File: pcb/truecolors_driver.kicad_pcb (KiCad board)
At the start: 4 copper layers, 70 x 90 mm, 66 parts, among them Q1 AOD413A(UMW), Q2 AOD413A(UMW), Q3 AOD413A(UMW), SW1 TS-1088-AR02016, U2 CH224A, U3 ESP32-S3-WROOM-1(N8R8), U4 AMS1117-3.3, U5 LM3409MY/NOPB, U6 LM3409MY/NOPB, U7 LM3409MY/NOPB

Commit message: update pcb
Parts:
- added C34: 10uF 25V, Capacitor_SMD:C_0603_1608Metric, F.Cu at (192.3, 124.2)
- added C35: 100nF 16V, Capacitor_SMD:C_0603_1608Metric, F.Cu at (191.1, 129.1)
- added C36: 10uF 25V, Capacitor_SMD:C_0603_1608Metric, F.Cu at (189.3, 119.7)
- added C37: 10uF 25V, Capacitor_SMD:C_0603_1608Metric, F.Cu at (189.3, 121.2)
- added C38: 10uF 25V, Capacitor_SMD:C_0603_1608Metric, F.Cu at (189.3, 122.7)
- added C39: 10uF 25V, Capacitor_SMD:C_0603_1608Metric, F.Cu at (189.3, 124.2)
- added C40: 100nF 16V, Capacitor_SMD:C_0603_1608Metric, F.Cu at (150.8, 134.5)
- added CN1: 1.0-3PWT, EasyEDA:CONN-SMD_3P-P1.00_C3029342, F.Cu at (140.7, 104.0)
- added CN2: 47053-1000, EasyEDA:CONN-TH_47053-1000, F.Cu at (143.8, 139.0)
- added L4: 4.7uH, EasyEDA:IND-SMD_L4.4-W4.2, F.Cu at (186.7, 127.5)
- added Q4: BSS138, Package_TO_SOT_SMD:SOT-23, F.Cu at (151.1, 140.0)
- added R17: 10k, Resistor_SMD:R_0603_1608Metric, F.Cu at (157.8, 85.1)
- added R18: 10k, Resistor_SMD:R_0603_1608Metric, F.Cu at (180.2, 85.1)
- added R19: 10k, Resistor_SMD:R_0603_1608Metric, F.Cu at (202.5, 85.1)
- added R20: 10k, Resistor_SMD:R_0603_1608Metric, F.Cu at (150.8, 133.1)
- added R21: 68k, Resistor_SMD:R_0603_1608Metric, F.Cu at (150.8, 136.0)
- added R22: 2k2, Resistor_SMD:R_0603_1608Metric, F.Cu at (168.2, 125.0)
- added R23: 2k2, Resistor_SMD:R_0603_1608Metric, F.Cu at (166.7, 125.0)
- added R24: 120k, Resistor_SMD:R_0603_1608Metric, F.Cu at (200.2, 126.5)
- added R25: 10k, Resistor_SMD:R_0603_1608Metric, F.Cu at (147.7, 134.0)
- added R26: 120k, Resistor_SMD:R_0603_1608Metric, F.Cu at (154.5, 138.3)
- added U1: AP63205WU-7, EasyEDA:TSOT-23-6_L2.9-W1.6-P0.95-LS2.8-BL, F.Cu at (191.8, 126.7)
- C1: value 1uF -> 1uF 50V; footprint Capacitor_SMD:C_0603_1608Metric_Pad1.08x0.95mm_HandSolder -> Capacitor_SMD:C_0603_1608Metric
- C10, C11, C12, C13, C14, C15, C16, C19, C20, C21, C22, C23, C24, C25, C26, C29, C30, C31, C32, C33, C4, C5, C6, C9: value 4.7uF -> 4.7uF 35V
- C17, C27, C7: value 1uF -> 1uF 50V
- C18, C28, C8: value 470pF -> 470pF 50V
- C2, C3: value 10uF -> 10uF 25V; footprint Capacitor_SMD:C_0603_1608Metric_Pad1.08x0.95mm_HandSolder -> Capacitor_SMD:C_0603_1608Metric
- moved C2 25.9 mm to (176.3, 137.8), turned to -90 degrees
- moved U4 21.2 mm to (170.6, 138.8), turned to 0 degrees
- moved C3 20.3 mm to (164.9, 140.1), turned to 180 degrees
- moved C1 2.59 mm to (205.7, 116.7), turned to 90 degrees
- moved C18 1.53 mm to (178.2, 82.8), turned to 180 degrees
- moved C28 1.53 mm to (200.6, 82.8), turned to 180 degrees
- moved C8 1.53 mm to (155.8, 82.8), turned to 180 degrees
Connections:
- U2 pad 10: /PD_PG -> unconnected-(U2-PG-Pad10)
- U2 pad 2: unconnected-(U2-CFG2/SCL-Pad2) -> /CH224A_SCL
- U2 pad 3: unconnected-(U2-CFG3/SDA-Pad3) -> /CH224A_SDA
- U2 pad 9: GND -> Net-(U2-CFG1)
- U3 pad 12: unconnected-(U3-IO8-Pad12) -> /CH224A_SDA
- U3 pad 17: unconnected-(U3-IO9-Pad17) -> /CH224A_SCL
- U3 pad 31: unconnected-(U3-IO38-Pad31) -> /EN_B
- U3 pad 32: unconnected-(U3-IO39-Pad32) -> /EN_G
- U3 pad 33: unconnected-(U3-IO40-Pad33) -> /EN_R
- U3 pad 4: unconnected-(U3-IO4-Pad4) -> /VIN_ADC
- U3 pad 6: unconnected-(U3-IO6-Pad6) -> /FAN_PWM
- U3 pad 7: unconnected-(U3-IO7-Pad7) -> /FAN_TACH
- U5 pad 3: /driverR/PWM -> /EN_R
- U6 pad 3: /driverG/PWM -> /EN_G
- U7 pad 3: /driverB/PWM -> /EN_B
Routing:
- net /EN_B: track 0.00 -> 70.9 mm
- net /CH224A_SDA: track 0.00 -> 57.8 mm, vias 0 -> 3
- net /CH224A_SCL: track 0.00 -> 53.9 mm, vias 0 -> 2
- net +20V: track 83.5 -> 135.7 mm, vias 21 -> 24
- net /EN_G: track 0.00 -> 49.9 mm
- net +5V: track 2.90 -> 50.8 mm, vias 0 -> 7
- net /EN_R: track 0.00 -> 31.6 mm
- net /FAN_TACH: track 0.00 -> 18.5 mm, vias 0 -> 1
- net /FAN_PWM: track 0.00 -> 13.4 mm
- net /RX: track 0.00 -> 13.2 mm
- net /TX: track 0.00 -> 11.0 mm
- net GND: track 2.77 -> 11.9 mm, vias 15 -> 29
- net Net-(U2-CFG1): track 0.00 -> 5.75 mm
- net Net-(U1-SW): track 0.00 -> 4.50 mm
- net /VIN_ADC: track 0.00 -> 4.48 mm
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- added copper zone on In2.Cu, net +5V

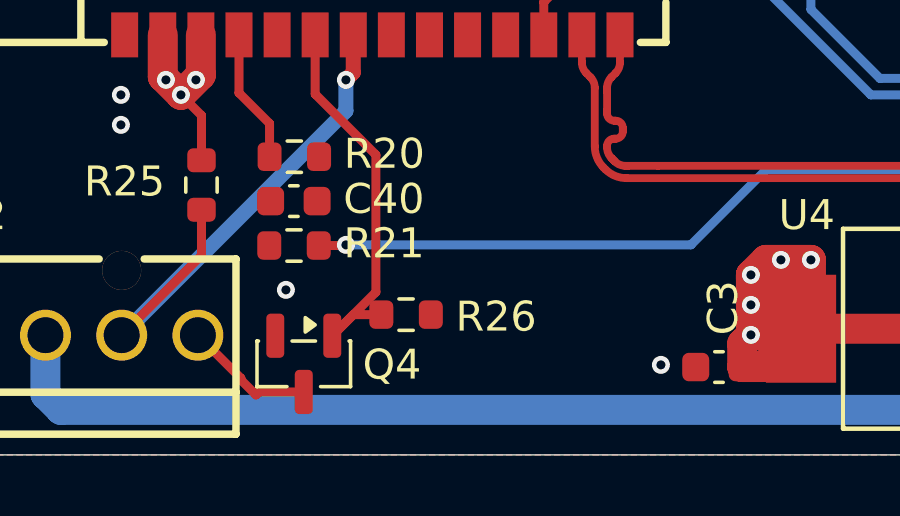
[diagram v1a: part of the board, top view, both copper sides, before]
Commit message: R26 pullup instead of pulldown for fan-off boot
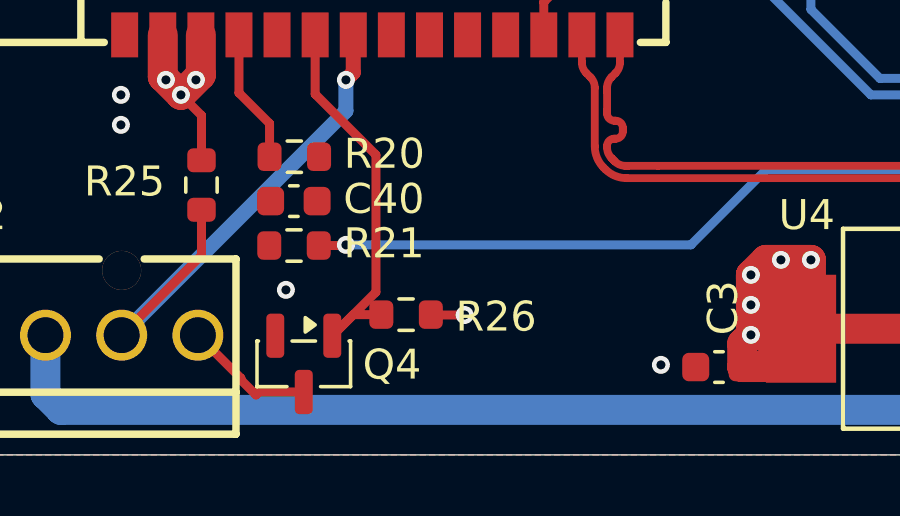
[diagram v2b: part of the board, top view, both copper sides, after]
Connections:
- R26 pad 2: GND -> +3.3V
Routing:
- net +3.3V: track 36.5 -> 37.6 mm, vias 10 -> 11
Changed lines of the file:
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@@
 			(layers "F.Cu" "F.Mask" "F.Paste")
 			(roundrect_rratio 0.25)
-			(net "GND")
+			(net "+3.3V")
 			(pintype "passive")
 		)
@@
 		(sheetname "/")
 		(sheetfile "truecolors_driver.kicad_sch")
+		(units
+			(unit
+				(name "A")
+				(pins "1" "2" "3" "4" "5" "11" "10" "9" "8" "7" "6")
+			)
+		)
 		(attr smd)
 		(duplicate_pad_numbers_are_jumpers no)
@@
 	)
 	(segment
+		(start 156.458288 138.337116)
+		(end 155.342116 138.337116)
+		(width 0.3)
+		(layer "F.Cu")
+		(net "+3.3V")
+	)
+	(segment
 		(start 147.665 129)
 		(end 147.665 130.335)
@@
 	)
 	(segment
+		(start 155.342116 138.337116)
+		(end 155.33 138.325)
+		(width 0.3)
+		(layer "F.Cu")
+		(net "+3.3V")
+	)
+	(segment
 		(start 168 136.5)
 		(end 166.5 136.5)
@@
 		(size 0.6)
 		(drill 0.3)
+		(layers "F.Cu" "B.Cu")
+		(free yes)
+		(net "+3.3V")
+	)
+	(via
+		(at 156.458288 138.337116)
+		(size 0.6)
+		(drill 0.3)

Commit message: add mic, add ntc, fix all drc errors
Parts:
- added C41: 100nF 16V, Capacitor_SMD:C_0603_1608Metric, F.Cu at (93.6, 122.2)
- added C42: 10uF 25V, Capacitor_SMD:C_0603_1608Metric, F.Cu at (95.2, 122.2)
- added C43: 100nF 16V, Capacitor_SMD:C_0603_1608Metric, F.Cu at (86.2, 60.8)
- added MIC1: MSM261DGT003, EasyEDA:MIC-SMD_6P-L4.0-W2.0_LMD4020T261-OC3, F.Cu at (90.6, 122.2)
- added R27: 10k, Resistor_SMD:R_0603_1608Metric, F.Cu at (89.3, 125.4)
- added TP1: NTC+, TestPoint:TestPoint_Keystone_5019_Miniature, F.Cu at (83.0, 57.6)
- added TP2: NTC-, TestPoint:TestPoint_Keystone_5019_Miniature, F.Cu at (86.4, 57.6)
- added TP3: R+, TestPoint:TestPoint_Keystone_5019_Miniature, F.Cu at (74.0, 57.6)
- added TP4: GND, TestPoint:TestPoint_Keystone_5019_Miniature, F.Cu at (70.4, 57.6)
- added TP5: G+, TestPoint:TestPoint_Keystone_5019_Miniature, F.Cu at (96.4, 57.6)
- added TP6: GND, TestPoint:TestPoint_Keystone_5019_Miniature, F.Cu at (92.8, 57.6)
- added TP7: B+, TestPoint:TestPoint_Keystone_5019_Miniature, F.Cu at (118.8, 57.6)
- added TP8: GND, TestPoint:TestPoint_Keystone_5019_Miniature, F.Cu at (115.2, 57.6)
- moved R22 76.7 mm to (91.7, 131.5), turned to 90 degrees
- moved R23 76.7 mm to (90.3, 131.5), turned to 90 degrees
- moved C13 76.5 mm to (71.4, 87.4)
- moved C8 76.5 mm to (79.3, 84.8)
- moved R2 76.5 mm to (79.6, 90.1)
- moved R3 76.5 mm to (74.8, 95.1)
- moved SW1 76.5 mm to (89.7, 110.4)
- moved U1 76.5 mm to (115.3, 128.7)
- moved C1 76.5 mm to (129.2, 118.7)
- moved C11 76.5 mm to (67.3, 63.7)
- moved C2 76.5 mm to (99.8, 139.8)
- moved C3 76.5 mm to (88.4, 142.1)
- moved C35 76.5 mm to (114.6, 131.1)
- moved C4 76.5 mm to (73.8, 89.6)
- moved C40 76.5 mm to (74.3, 136.5)
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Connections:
- net Net-(U3-IO0) renamed /BOOT
- U3 pad 18: unconnected-(U3-IO10-Pad18) -> /NTC_ADC
- U3 pad 20: unconnected-(U3-IO12-Pad20) -> /MIC_CLK
- U3 pad 21: unconnected-(U3-IO13-Pad21) -> /MIC_DATA
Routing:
- net /NTC_ADC: track 0.00 -> 73.7 mm, vias 0 -> 2
- net +3.3V: track 37.6 -> 43.5 mm, vias 11 -> 13
- net /driverB/VOUT: track 29.2 -> 34.3 mm
- net /driverG/VOUT: track 29.2 -> 34.3 mm
- net /driverR/VOUT: track 29.2 -> 34.3 mm
- net /MIC_CLK: track 0.00 -> 3.33 mm
- net /MIC_DATA: track 0.00 -> 3.29 mm
- net /VIN_ADC: track 4.48 -> 7.48 mm
- net +20V: track 135.7 -> 137.2 mm
- net +5V: vias 7 -> 8
- net GND: vias 29 -> 39
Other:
- rule pad_to_mask_clearance: 0 -> 0.05

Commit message: refactor schematic
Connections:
- net /CC1 renamed /power/CC1
- net /CC2 renamed /power/CC2
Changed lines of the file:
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@@
 		)
 		(property ki_fp_filters "C_*")
-		(sheetname "/")
-		(sheetfile "truecolors_driver.kicad_sch")
+		(sheetname "/power/")
+		(sheetfile "power.kicad_sch")
 		(units
 			(unit
@@
 		)
 		(property ki_fp_filters "R_*")
-		(sheetname "/")
-		(sheetfile "truecolors_driver.kicad_sch")
+		(sheetname "/power/")
+		(sheetfile "power.kicad_sch")
 		(units
 			(unit
@@
 		)
 		(property ki_fp_filters "R_*")
-		(sheetname "/")
-		(sheetfile "truecolors_driver.kicad_sch")
+		(sheetname "/power/")
+		(sheetfile "power.kicad_sch")
 		(units
 			(unit
@@
 		)
 		(property ki_fp_filters "C_*")
-		(sheetname "/")
-		(sheetfile "truecolors_driver.kicad_sch")
+		(sheetname "/power/")
+		(sheetfile "power.kicad_sch")
 		(units
 			(unit
@@
 		(sheetname "/driverB/")
 		(sheetfile "numb12_driver.kicad_sch")
+		(units
+			(unit
+				(name "A")
+				(pins "1" "2" "3" "4" "5" "11" "10" "9" "8" "7" "6")
+			)
+		)
 		(attr smd)
 		(duplicate_pad_numbers_are_jumpers no)
@@
 		)
 		(property ki_fp_filters "C_*")
-		(sheetname "/")
-		(sheetfile "truecolors_driver.kicad_sch")
+		(sheetname "/power/")
+		(sheetfile "power.kicad_sch")
 		(units
 			(unit
@@
 			)
 		)
-		(sheetname "/")
-		(sheetfile "truecolors_driver.kicad_sch")
+		(sheetname "/power/")
+		(sheetfile "power.kicad_sch")
 		(units
 			(unit
@@
 		(sheetname "/driverR/")
 		(sheetfile "numb12_driver.kicad_sch")
+		(units
+			(unit
+				(name "A")
+				(pins "1" "2" "3" "4" "5" "11" "10" "9" "8" "7" "6")
+			)
+		)
 		(attr smd)
 		(duplicate_pad_numbers_are_jumpers no)
@@
 		)
 		(property ki_fp_filters "C_*")
-		(sheetname "/")
-		(sheetfile "truecolors_driver.kicad_sch")
+		(sheetname "/power/")
+		(sheetfile "power.kicad_sch")
 		(units
 			(unit
@@
 		(sheetname "/")
 		(sheetfile "truecolors_driver.kicad_sch")
+		(units
+			(unit
+				(name "A")
+				(pins "1" "2" "3" "4")
+			)
+		)
 		(attr through_hole)
 		(duplicate_pad_numbers_are_jumpers no)
@@
 		)
 		(property ki_fp_filters "C_*")
-		(sheetname "/")
-		(sheetfile "truecolors_driver.kicad_sch")
+		(sheetname "/power/")
+		(sheetfile "power.kicad_sch")
 		(units
 			(unit
@@
 		(sheetname "/driverG/")
 		(sheetfile "numb12_driver.kicad_sch")
+		(units
+			(unit
+				(name "A")
+				(pins "1" "2" "3" "4" "5" "11" "10" "9" "8" "7" "6")
+			)
+		)
 		(attr smd)
 		(duplicate_pad_numbers_are_jumpers no)
@@
 		)
 		(property ki_fp_filters "C_*")
-		(sheetname "/")
-		(sheetfile "truecolors_driver.kicad_sch")
+		(sheetname "/power/")
+		(sheetfile "power.kicad_sch")
 		(units
 			(unit
@@
 			)
 		)
-		(sheetname "/")
-		(sheetfile "truecolors_driver.kicad_sch")
+		(sheetname "/power/")
+		(sheetfile "power.kicad_sch")
+		(units
+			(unit
+				(name "A")
+				(pins "1" "2" "3" "4" "5" "11" "10" "9" "8" "7" "6")
+			)
+		)
 		(attr smd)
 		(duplicate_pad_numbers_are_jumpers no)
@@
 			(size 1.5 0.6)
 			(layers "F.Cu" "F.Mask" "F.Paste")
-			(net "/CC2")
+			(net "/power/CC2")
 			(pinfunction "CC2_6")
 			(pintype "unspecified")
@@
 			(size 1.5 0.6)
 			(layers "F.Cu" "F.Mask" "F.Paste")
-			(net "/CC1")
+			(net "/power/CC1")
 			(pinfunction "CC1_7")
 			(pintype "unspecified")
@@
 			)
 		)
-		(sheetname "/")
-		(sheetfile "truecolors_driver.kicad_sch")
+		(sheetname "/power/")
+		(sheetfile "power.kicad_sch")
 		(units
 			(unit
@@
 		)
 		(property ki_fp_filters "R_*")
-		(sheetname "/")
-		(sheetfile "truecolors_driver.kicad_sch")
+		(sheetname "/power/")
+		(sheetfile "power.kicad_sch")
 		(units
 			(unit
@@
 			)
 		)
-		(sheetname "/")
-		(sheetfile "truecolors_driver.kicad_sch")
+		(sheetname "/power/")
+		(sheetfile "power.kicad_sch")
 		(units
 			(unit
@@
 		)
 		(property ki_fp_filters "C_*")
-		(sheetname "/")
-		(sheetfile "truecolors_driver.kicad_sch")
+		(sheetname "/power/")
+		(sheetfile "power.kicad_sch")
 		(units
 			(unit
@@
 			(net "unconnected-(U3-IO5-Pad5)")
 			(pinfunction "IO5_5")
-			(pintype "unspecified")
+			(pintype "unspecified+no_connect")
 		)
 		(pad "6" smd rect
@@
 			(net "unconnected-(U3-IO15-Pad8)")
 			(pinfunction "IO15_8")
-			(pintype "unspecified")
+			(pintype "unspecified+no_connect")
 		)
 		(pad "9" smd rect
@@
 			(net "unconnected-(U3-IO16-Pad9)")
 			(pinfunction "IO16_9")
-			(pintype "unspecified")
+			(pintype "unspecified+no_connect")
 		)
 		(pad "10" smd rect
@@
 			(net "unconnected-(U3-IO17-Pad10)")
 			(pinfunction "IO17_10")
-			(pintype "unspecified")
+			(pintype "unspecified+no_connect")
 		)
 		(pad "11" smd rect
@@
 			(net "unconnected-(U3-IO18-Pad11)")
 			(pinfunction "IO18_11")
-			(pintype "unspecified")
+			(pintype "unspecified+no_connect")
 		)
 		(pad "12" smd rect
@@
 			(net "unconnected-(U3-IO3-Pad15)")
 			(pinfunction "IO3_15")
-			(pintype "unspecified")
+			(pintype "unspecified+no_connect")
 		)
 		(pad "16" smd rect
@@
 			(net "unconnected-(U3-IO46-Pad16)")
 			(pinfunction "IO46_16")
-			(pintype "unspecified")
+			(pintype "unspecified+no_connect")
 		)
 		(pad "17" smd rect
@@
 			(net "unconnected-(U3-IO11-Pad19)")
 			(pinfunction "IO11_19")
-			(pintype "unspecified")
+			(pintype "unspecified+no_connect")
 		)
 		(pad "20" smd rect
@@
 			(net "unconnected-(U3-IO14-Pad22)")
 			(pinfunction "IO14_22")
-			(pintype "unspecified")
+			(pintype "unspecified+no_connect")
 		)
 		(pad "23" smd rect
@@
 			(net "unconnected-(U3-IO21-Pad23)")
 			(pinfunction "IO21_23")
-			(pintype "unspecified")
+			(pintype "unspecified+no_connect")
 		)
 		(pad "24" smd rect
@@
 			(net "unconnected-(U3-IO47-Pad24)")
 			(pinfunction "IO47_24")
-			(pintype "unspecified")
+			(pintype "unspecified+no_connect")
 		)
 		(pad "25" smd rect
@@
 			(net "unconnected-(U3-IO48-Pad25)")
 			(pinfunction "IO48_25")
-			(pintype "unspecified")
+			(pintype "unspecified+no_connect")
 		)
 		(pad "26" smd rect
@@
 			(net "unconnected-(U3-IO45-Pad26)")
 			(pinfunction "IO45_26")
-			(pintype "unspecified")
+			(pintype "unspecified+no_connect")
 		)
 		(pad "27" smd rect
@@
 			(net "unconnected-(U3-IO35-Pad28)")
 			(pinfunction "IO35_28")
-			(pintype "unspecified")
+			(pintype "unspecified+no_connect")
 		)
 		(pad "29" smd rect
@@
 			(net "unconnected-(U3-IO36-Pad29)")
 			(pinfunction "IO36_29")
-			(pintype "unspecified")
+			(pintype "unspecified+no_connect")
 		)
 		(pad "30" smd rect
@@
 			(net "unconnected-(U3-IO37-Pad30)")
 			(pinfunction "IO37_30")
-			(pintype "unspecified")
+			(pintype "unspecified+no_connect")
 		)
 		(pad "31" smd rect
@@
 			(net "unconnected-(U3-IO41-Pad34)")
 			(pinfunction "IO41_34")
-			(pintype "unspecified")
+			(pintype "unspecified+no_connect")
 		)
 		(pad "35" smd rect
@@
 			(net "unconnected-(U3-IO42-Pad35)")
 			(pinfunction "IO42_35")
-			(pintype "unspecified")
+			(pintype "unspecified+no_connect")
 		)
 		(pad "36" smd rect
@@
 			(net "unconnected-(U3-IO2-Pad38)")
 			(pinfunction "IO2_38")
-			(pintype "unspecified")
+			(pintype "unspecified+no_connect")
 		)
 		(pad "39" smd rect
@@
 			(net "unconnected-(U3-IO1-Pad39)")
 			(pinfunction "IO1_39")
-			(pintype "unspecified")
+			(pintype "unspecified+no_connect")
 		)
 		(pad "40" smd rect
@@
 			)
 		)
-		(sheetname "/")
-		(sheetfile "truecolors_driver.kicad_sch")
+		(sheetname "/power/")
+		(sheetfile "power.kicad_sch")
+		(units
+			(unit
+				(name "A")
+				(pins "A1B12" "A4B9" "B8" "A5" "B7" "A6" "A7" "B6" "A8" "B5" "B4A9" "B1A12"
+					"4" "3" "2" "1"
+				)
+			)
+		)
 		(attr smd)
 		(duplicate_pad_numbers_are_jumpers no)
@@
 			(size 0.3 1.3)
 			(layers "F.Cu" "F.Mask" "F.Paste")
-			(net "/CC1")
+			(net "/power/CC1")
 			(pinfunction "CC1_A5")
 			(pintype "unspecified")
@@
 			(size 0.3 1.3)
 			(layers "F.Cu" "F.Mask" "F.Paste")
-			(net "/CC2")
+			(net "/power/CC2")
 			(pinfunction "CC2_B5")
 			(pintype "unspecified")
@@
 		)
 		(property ki_fp_filters "C_*")
-		(sheetname "/")
-		(sheetfile "truecolors_driver.kicad_sch")
+		(sheetname "/power/")
+		(sheetfile "power.kicad_sch")
 		(units
 			(unit
@@
 		)
 		(property ki_fp_filters "C_*")
-		(sheetname "/")
-		(sheetfile "truecolors_driver.kicad_sch")
+		(sheetname "/power/")
+		(sheetfile "power.kicad_sch")
 		(units
 			(unit
@@
 	)
 	(segment
-		(start 124.68 134.32)
-		(end 125.015348 133.984652)
-		(width 0.2)
-		(layer "F.Cu")
-		(net "/CC2")
-	)
-	(segment
-		(start 122.7 134.32)
-		(end 124.68 134.32)
-		(width 0.2)
-		(layer "F.Cu")
-		(net "/CC2")
-	)
-	(segment
-		(start 125.015348 133.984652)
-		(end 125.015348 128.454788)
-		(width 0.2)
-		(layer "F.Cu")
-		(net "/CC2")
-	)
-	(segment
-		(start 126.015348 128.454788)
-		(end 126.015348 134.854652)
-		(width 0.2)
-		(layer "F.Cu")
-		(net "/CC1")
-	)
-	(segment
-		(start 123.55 137.32)
-		(end 122.7 137.32)
-		(width 0.2)
-		(layer "F.Cu")
-		(net "/CC1")
-	)
-	(segment
-		(start 126.015348 134.854652)
-		(end 123.55 137.32)
-		(width 0.2)
-		(layer "F.Cu")
-		(net "/CC1")
-	)
-	(segment
 		(start 122.7 135.82)
 		(end 121.724999 135.82)
@@
 		(net "/BOOT")
 	)
+	(segment
+		(start 124.68 134.32)
+		(end 125.015348 133.984652)
+		(width 0.2)
+		(layer "F.Cu")
+		(net "/power/CC2")
+	)
+	(segment
+		(start 122.7 134.32)
+		(end 124.68 134.32)
+		(width 0.2)
+		(layer "F.Cu")
+		(net "/power/CC2")
+	)
+	(segment
+		(start 125.015348 133.984652)
+		(end 125.015348 128.454788)
+		(width 0.2)
+		(layer "F.Cu")
+		(net "/power/CC2")
+	)
+	(segment
+		(start 126.015348 128.454788)
+		(end 126.015348 134.854652)
+		(width 0.2)
+		(layer "F.Cu")
+		(net "/power/CC1")
+	)
+	(segment
+		(start 123.55 137.32)
+		(end 122.7 137.32)
+		(width 0.2)
+		(layer "F.Cu")
+		(net "/power/CC1")
+	)
+	(segment
+		(start 126.015348 134.854652)
+		(end 123.55 137.32)
+		(width 0.2)
+		(layer "F.Cu")
+		(net "/power/CC1")
+	)
 	(zone

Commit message: add mounting holes, labels
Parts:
- added H1: M3, MountingHole:MountingHole_3.2mm_M3_DIN965_Pad, F.Cu at (93.0, 116.0)
- added H2: M3, MountingHole:MountingHole_3.2mm_M3_DIN965_Pad, F.Cu at (103.5, 58.5)
- added H3: M3, MountingHole:MountingHole_3.2mm_M3_DIN965_Pad, F.Cu at (124.0, 116.0)
- added H4: M3, MountingHole:MountingHole_3.2mm_M3_DIN965_Pad, F.Cu at (127.0, 58.5)
- added H5: M3, MountingHole:MountingHole_3.2mm_M3_DIN965_Pad, F.Cu at (109.0, 141.5)
- moved SW1 5.62 mm to (85.4, 106.8), turned to -90 degrees
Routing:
- net /BOOT: track 5.59 -> 4.88 mm
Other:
- board text added: "CAUTION - CLASS 4 LASER RADIATION WHEN DISASSEMBLED AND DIFFUSOR OPTICS REMOVED"
- board text added: "True Colors 110% BT.2020 Mood Light 20V 3A 60W © 2026 whosmatt"

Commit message: finalize bom
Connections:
- H1 pad 1: (no net) -> unconnected-(H1-Pad1)
- H2 pad 1: (no net) -> unconnected-(H2-Pad1)
- H3 pad 1: (no net) -> unconnected-(H3-Pad1)
- H4 pad 1: (no net) -> unconnected-(H4-Pad1)
- H5 pad 1: (no net) -> unconnected-(H5-Pad1)
